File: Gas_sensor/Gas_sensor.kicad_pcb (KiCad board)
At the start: 2 copper layers, 143 parts, among them J1 Conn_02x02_Counter_Clockwise, J2 Conn_01x04, J3 Conn_01x10, J4 Conn_01x01, J5 Conn_01x01, Q1 DMC1229UFDB, Q2 DMC1229UFDB, Q3 Q_NMOS_GSD, Q4 Q_NMOS_GSD, Q5 Q_NMOS_GSD, Q6 Q_NMOS_GSD, SW1 SW_Push, SW10 SW_Push, SW11 SW_Push, SW12 SW_Push, SW2 SW_Push, SW3 SW_Push, SW4 SW_Push, SW5 SW_Push, SW6 SW_Push, SW7 SW_Push, SW8 SW_Push, SW9 SW_Push, U1 LPV511, U10 MCP1700-3302E_SOT23, U11 STM32F401CCUx, U12 TMP117, U13 TPS63070, U14 TPS79333-EP, U15 REG102GA, U2 LPV511, U3 MCP47CMB22, U4 MCP6V71, U5 LPV511, U6 MCP6V71, U7 MCP6V71, U8 MCP6V71, U9 ADS1115IDGS, Y1 25MHz

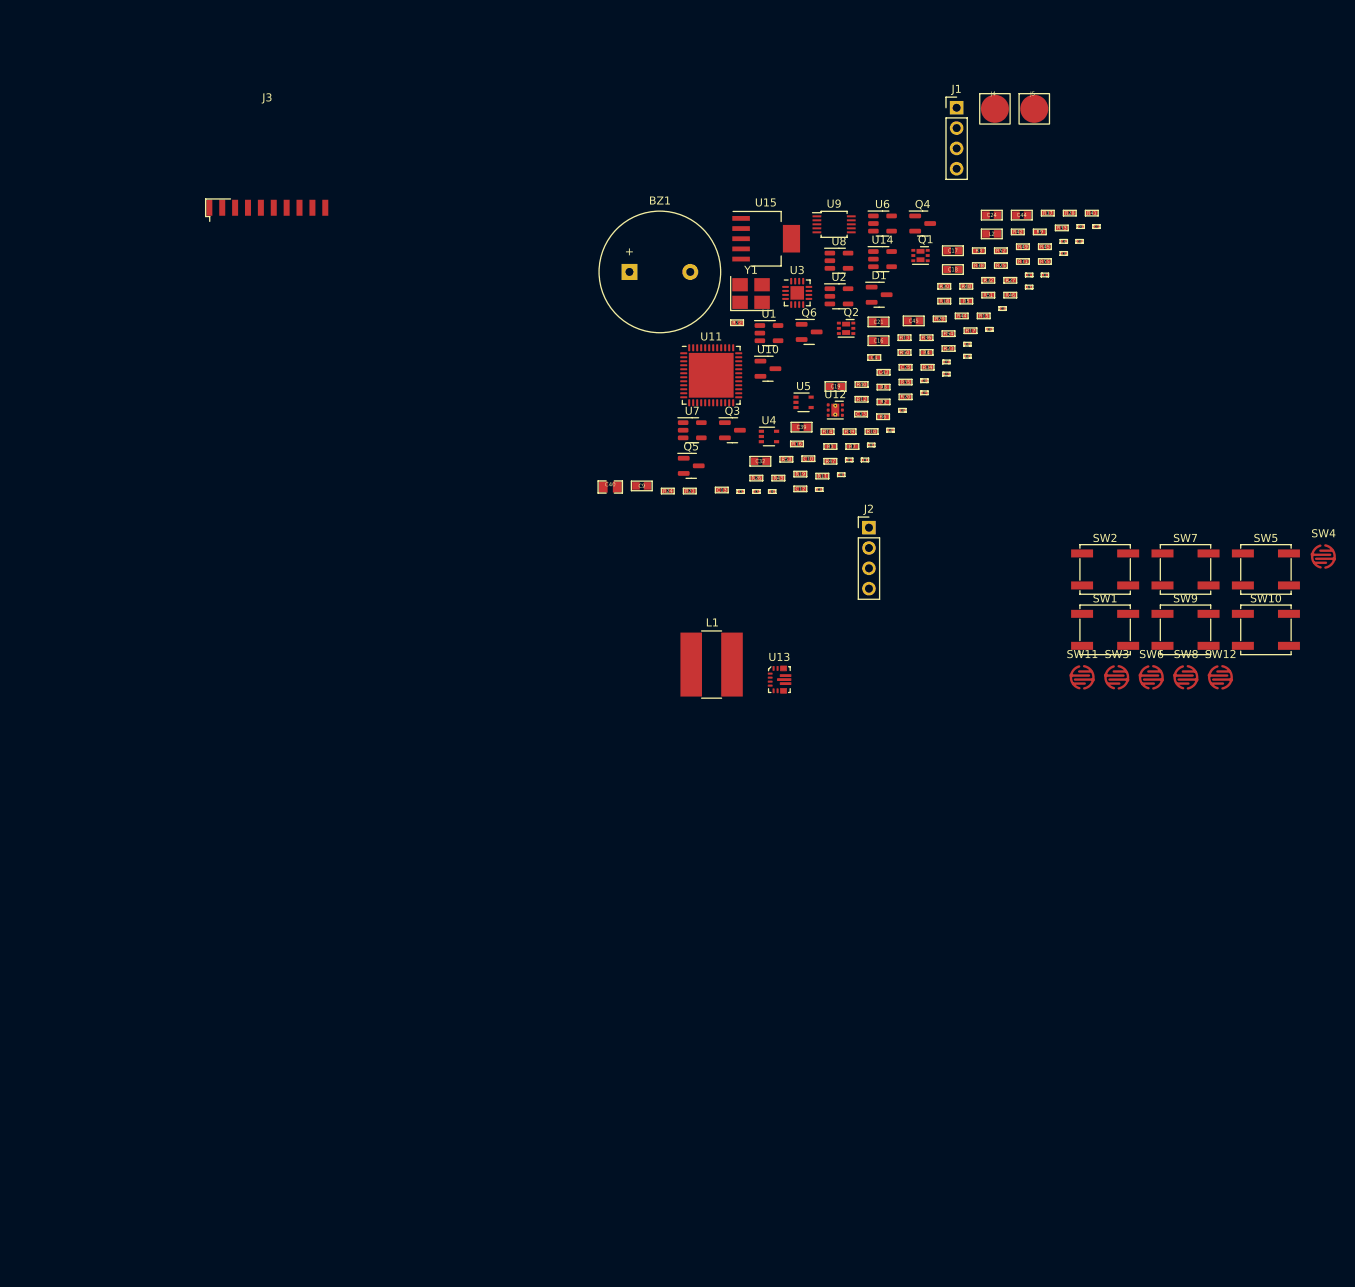
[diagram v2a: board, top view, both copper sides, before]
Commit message: Update layout, place switch
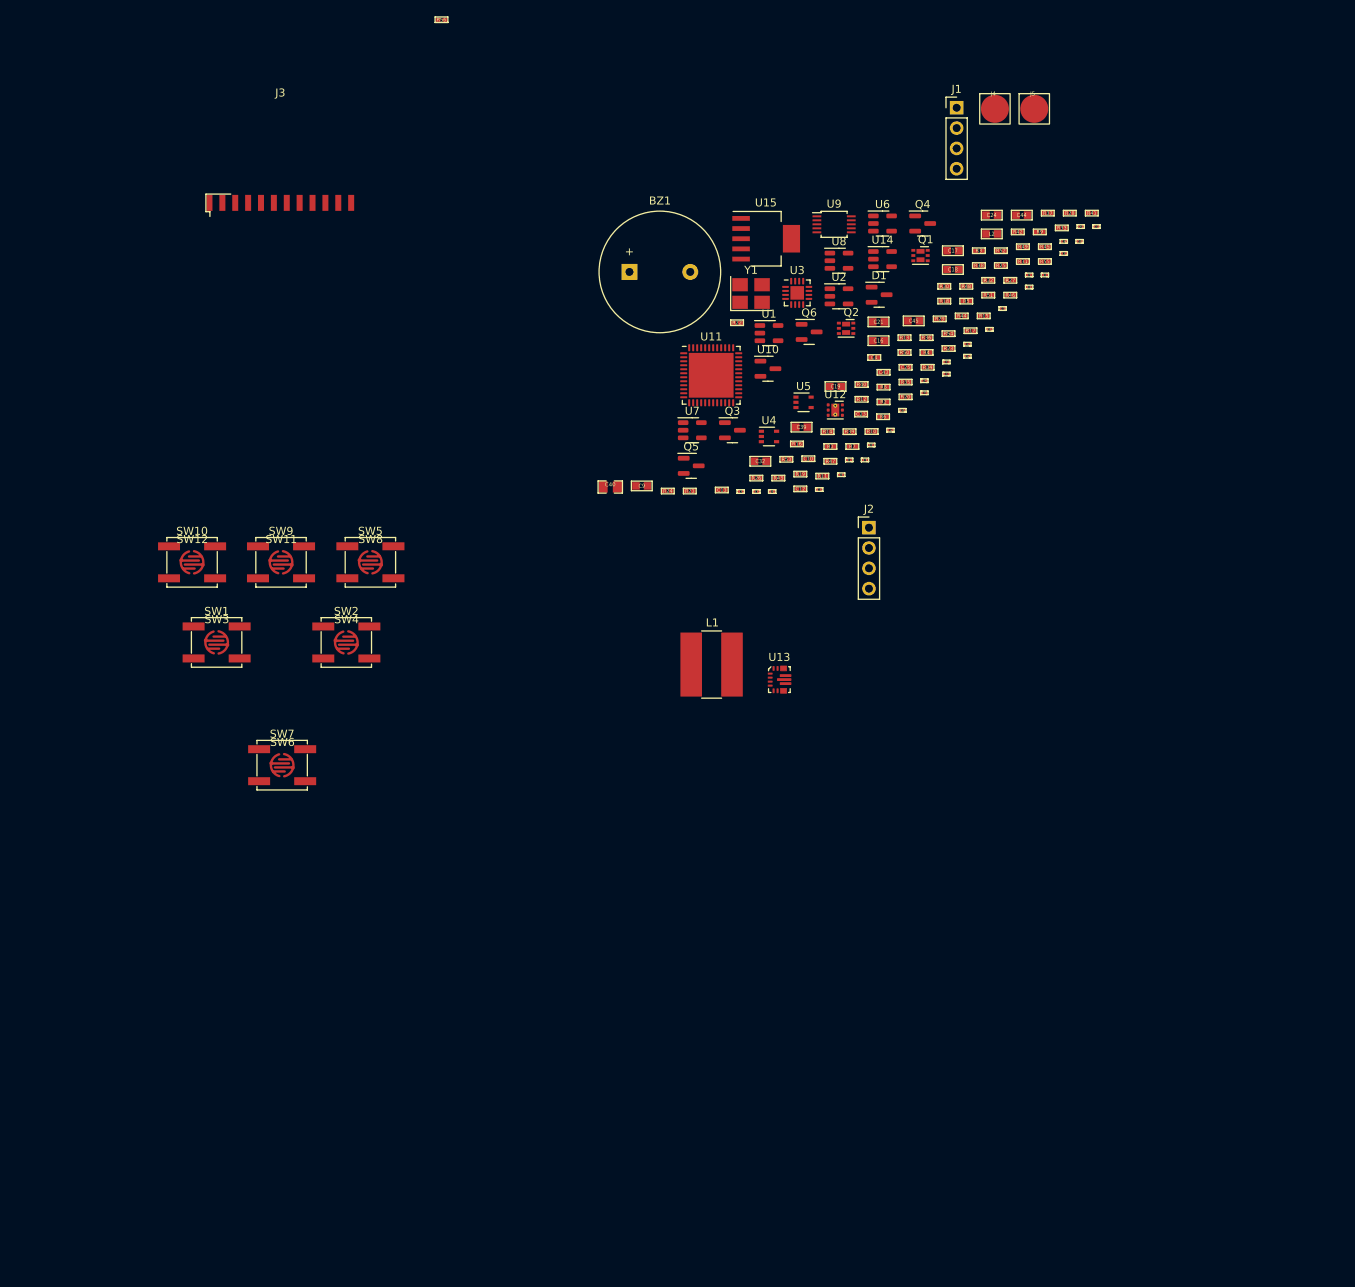
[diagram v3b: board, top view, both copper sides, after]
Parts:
- added R56: nc, Yame_library:SM0402-MR, F.Cu at (75.9, 23.7)
- J3: footprint Yame_library:LCD_Contact_1x10_P2.54mm -> Yame_library:LCD_Contact_1x12_P2.54mm
- moved SW10 134.5 mm to (44.8, 91.5)
- moved SW12 129.3 mm to (44.8, 91.5)
- moved SW4 122.6 mm to (64.0, 101.5)
- moved SW7 115.5 mm to (56.0, 116.9)
- moved SW9 113.4 mm to (55.9, 91.5)
- moved SW3 112.6 mm to (47.8, 101.5)
- moved SW5 111.9 mm to (67.0, 91.5)
- moved SW1 111.1 mm to (47.8, 101.5)
- moved SW6 109.2 mm to (56.0, 116.9)
- moved SW8 102.9 mm to (67.0, 91.5)
- moved SW11 101.2 mm to (55.9, 91.5)
- moved SW2 95.3 mm to (64.0, 101.5)
- moved J3 1.74 mm to (55.8, 46.6)
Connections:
- U11 pad 3: unconnected-(U11-Pad3) -> /Vseg6
- U11 pad 4: unconnected-(U11-Pad4) -> /Vseg7

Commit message: gas sensor : place components
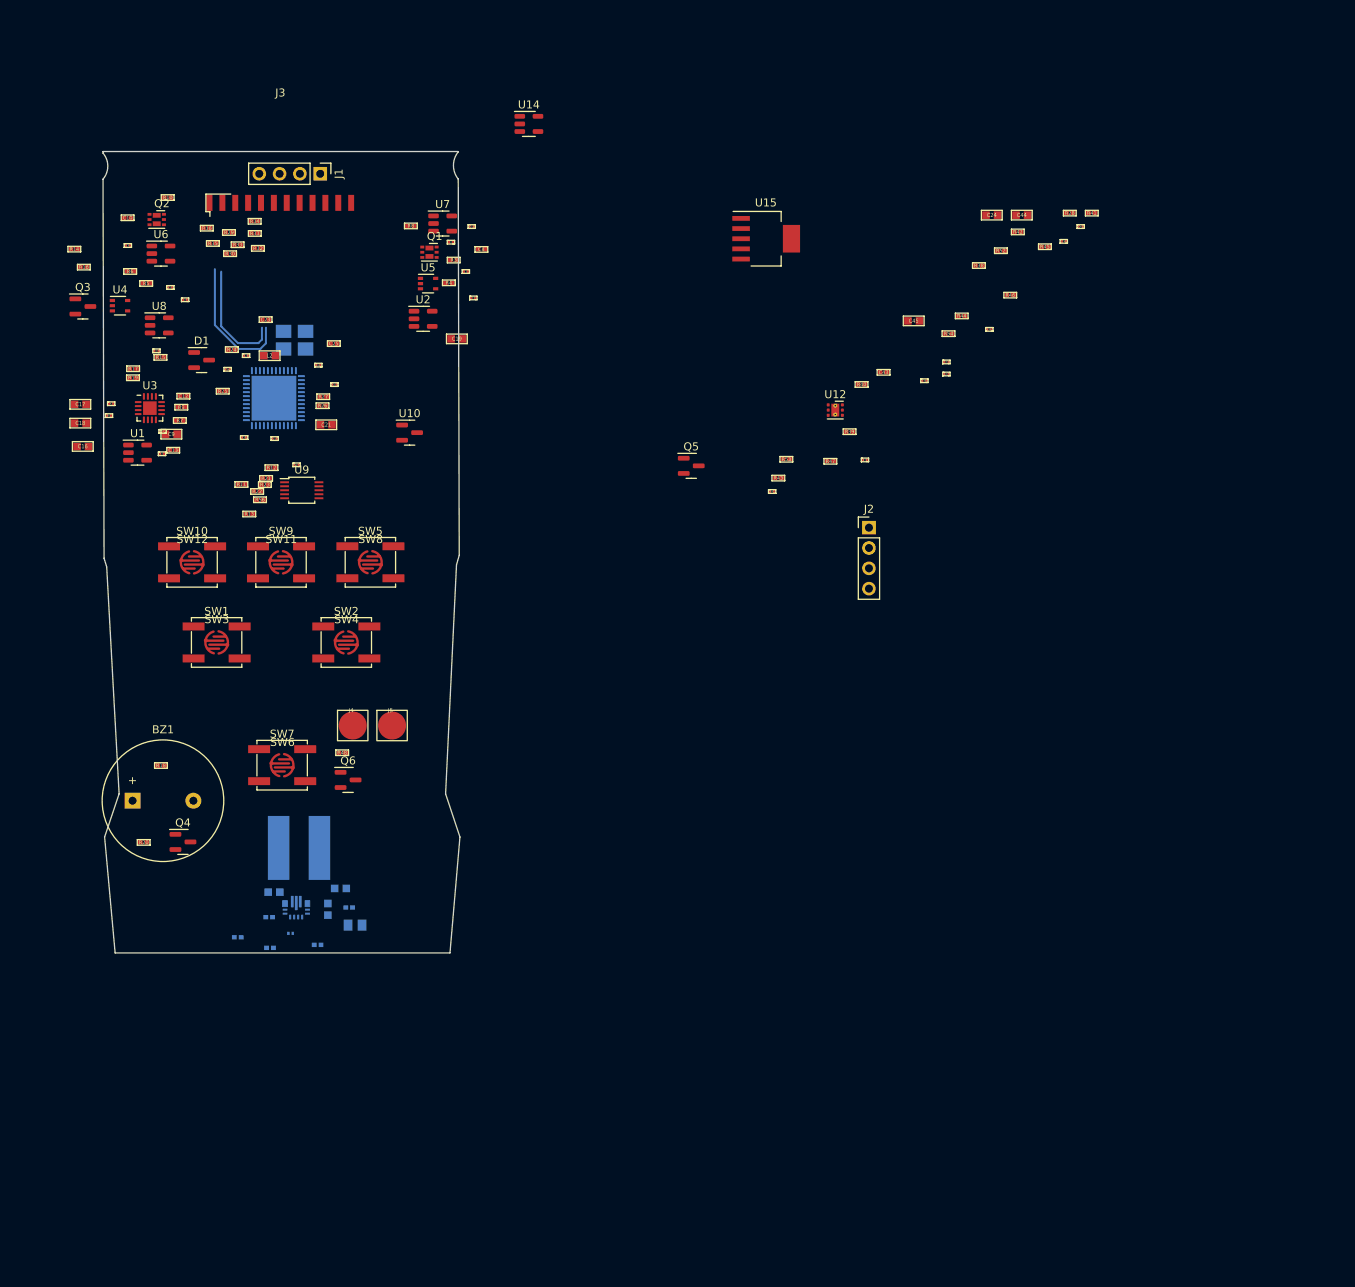
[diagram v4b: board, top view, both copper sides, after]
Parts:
- added C46: 10u, Yame_library:SM0603-MR, B.Cu at (63.3, 132.3)
- C32, C35, C39, C40, L1, R37, R49, R50, R51, R55, U11, U13, Y1: moved to B.Cu
- R1, R2: footprint Yame_library:SM0402-MR -> Yame_library:SM0201-MR
- moved R49 128.6 mm to (54.5, 139.7), turned to 180 degrees
- moved R55 124.7 mm to (60.5, 139.3), turned to 180 degrees
- moved R51 123.5 mm to (50.5, 138.4), turned to 180 degrees
- moved R37 123.1 mm to (64.4, 134.7), turned to 180 degrees
- moved Q4 120.5 mm to (43.6, 126.5)
- moved C14 116.2 mm to (40.3, 65.1)
- moved C5 114.8 mm to (41.1, 75.1)
- moved R18 113.8 mm to (40.9, 116.9)
- moved C6 112.7 mm to (36.7, 51.9)
- moved J4 111.3 mm to (64.8, 111.9)
- moved J5 111.3 mm to (69.8, 111.9)
- moved C17 110.7 mm to (30.8, 71.8)
- moved C18 110.7 mm to (30.8, 74.1)
- moved R20 110.3 mm to (38.7, 126.5)
- moved R9 109.5 mm to (43.4, 72.1)
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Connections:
- J1 pad 1: GND -> Net-(J1-Pad1)
- J1 pad 2: Net-(J1-Pad2) -> GND
- J1 pad 3: Net-(J1-Pad3) -> GND
- J1 pad 4: GND -> Net-(J1-Pad4)
- Q1 pad 3: Net-(J1-Pad2) -> Net-(J1-Pad1)
- Q1 pad 8: Net-(J1-Pad2) -> Net-(J1-Pad1)
- Q2 pad 3: Net-(J1-Pad3) -> Net-(J1-Pad4)
- Q2 pad 8: Net-(J1-Pad3) -> Net-(J1-Pad4)
- U7 pad 3: Net-(J1-Pad2) -> Net-(J1-Pad1)
- U8 pad 3: Net-(J1-Pad3) -> Net-(J1-Pad4)
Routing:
- net Net-(C26-Pad1): track 0.00 -> 16.9 mm
- net /Vcomm3: track 0.00 -> 14.5 mm
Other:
- board outline added: 44.6 x 100.2 mm
- copper layers 2 -> 4
- rule pad_to_mask_clearance: 0.2 -> 0.1

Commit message: update layout
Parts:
- removed C27: 100n, Yame_library:SM0201-MR
- removed D1: BAT54C, Package_TO_SOT_SMD:SOT-23
- C12, C13, C15, C19, C2, C20, C21, C22, C23, C24, C25, C26, C28, C29, C3, C30, C31, C4, C41, C42, C43, C44, C45, C5, C7, C9, J4, J5, L2, Q1, Q4, Q5, Q6, R1, R11, R12, R13, R18, R2, R20, R21, R22, R23, R25, R26, R27, R28, R29, R3, R30, R31, R32, R33, R34, R35, R36, R4, R40, R41, R42, R48, R56, R7, R8, R9, U1, U10, U12, U14, U15, U2, U3, U5, U7, U9: moved to B.Cu
- C16, C17, C18: footprint Yame_library:SM0603-MR -> Yame_library:SM0402-MR; moved to B.Cu
- R17, R19: footprint Yame_library:SM0402-MR -> Yame_library:SM0201-MR
- R24: footprint Yame_library:SM0402-MR -> Yame_library:SM0201-MR; moved to B.Cu
- Y1: footprint Oscillator:Oscillator_SMD_Abracon_ASE-4Pin_3.2x2.5mm_HandSoldering -> Crystal:Crystal_SMD_3225-4Pin_3.2x2.5mm
- moved R41 113.4 mm to (49.5, 83.2), turned to 90 degrees
- moved C44 109.5 mm to (57.9, 109.5), turned to 180 degrees
- moved C41 109.0 mm to (54.0, 88.3), turned to -90 degrees
- moved R42 103.3 mm to (49.5, 81.2), turned to 90 degrees
- moved C24 97.4 mm to (60.2, 96.5), turned to 90 degrees
- moved R28 88.1 mm to (67.5, 62.1), turned to -90 degrees
- moved C31 80.7 mm to (65.5, 79.4), turned to -90 degrees
- moved R40 80.6 mm to (49.5, 85.1), turned to 90 degrees
- moved C45 80.4 mm to (59.7, 89.5), turned to 90 degrees
- moved U15 79.5 mm to (57.3, 104.1), turned to 90 degrees
- moved C43 76.2 mm to (57.4, 86.8), turned to 180 degrees
- moved Q4 71.0 mm to (50.3, 55.7), turned to 180 degrees
- moved C42 68.1 mm to (54.5, 109.1), turned to 180 degrees
- moved Q5 60.6 mm to (46.5, 80.8), turned to 180 degrees
- moved U14 60.5 mm to (56.7, 89.2)
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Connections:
- C26 pad 1: Net-(C26-Pad1) -> +3V3
- U11 pad 1: Net-(C26-Pad1) -> +3V3
- U11 pad 20: unconnected-(U11-Pad20) -> /~{RDY}
- U11 pad 39: unconnected-(U11-Pad39) -> /APO
- U11 pad 46: /APO -> unconnected-(U11-Pad46)
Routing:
- net /Buzzer_EN: track 0.00 -> 53.2 mm
- net /Vcomm0: track 0.00 -> 27.5 mm
- net /Vcomm1: track 0.00 -> 27.0 mm
- net Net-(BZ1-Pad2): track 0.00 -> 25.1 mm
- net /Vseg0: track 0.00 -> 17.8 mm, vias 0 -> 1
- net Net-(C26-Pad1): track 16.9 -> 0.00 mm
- net /Vseg1: track 0.00 -> 13.5 mm
- net /Vseg5: track 0.00 -> 13.1 mm
- net /Vseg3: track 0.00 -> 12.6 mm
- net /Vseg4: track 0.00 -> 12.3 mm
- net /Vseg2: track 0.00 -> 12.3 mm
- net Net-(C23-Pad1): track 0.00 -> 12.1 mm
- net /Vcomm3: track 14.5 -> 24.7 mm
- net Net-(C25-Pad1): track 0.00 -> 6.73 mm
- net Net-(C20-Pad1): track 0.00 -> 2.59 mm
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
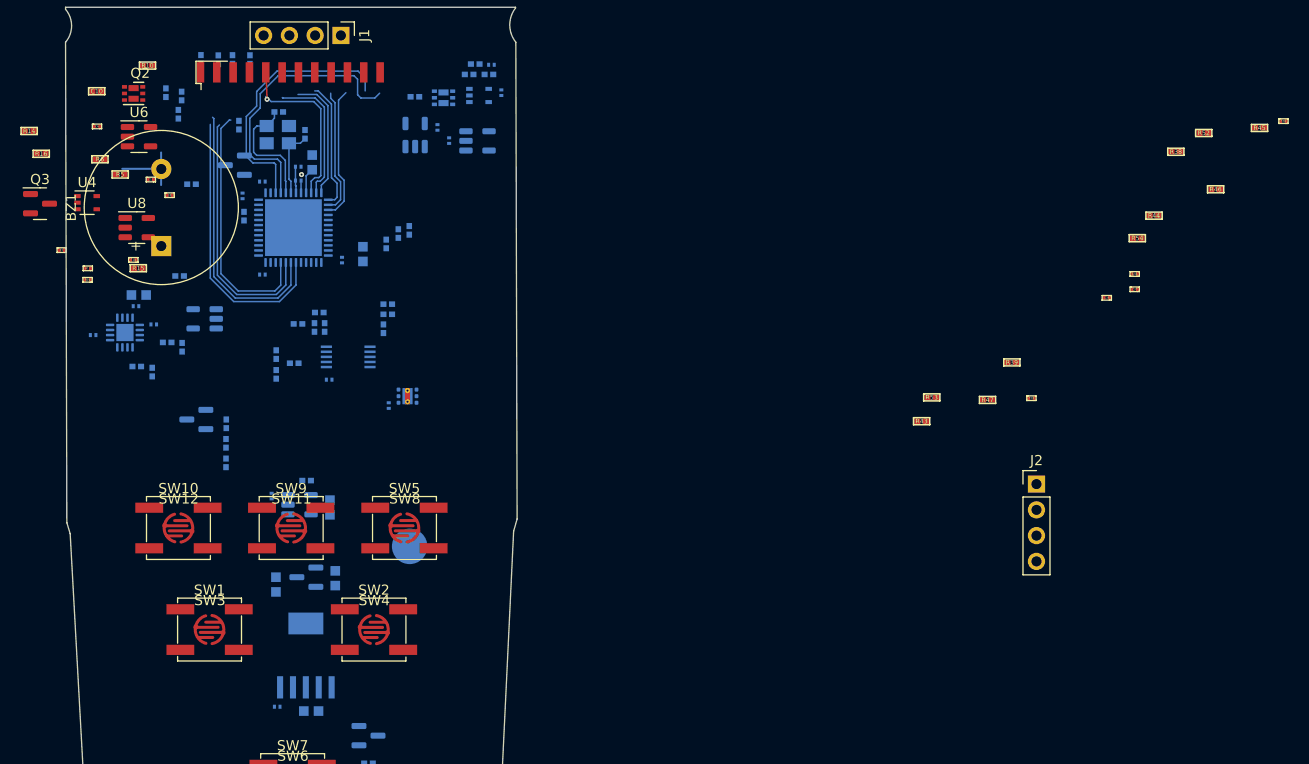
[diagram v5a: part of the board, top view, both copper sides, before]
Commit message: Gas sensor : update layout
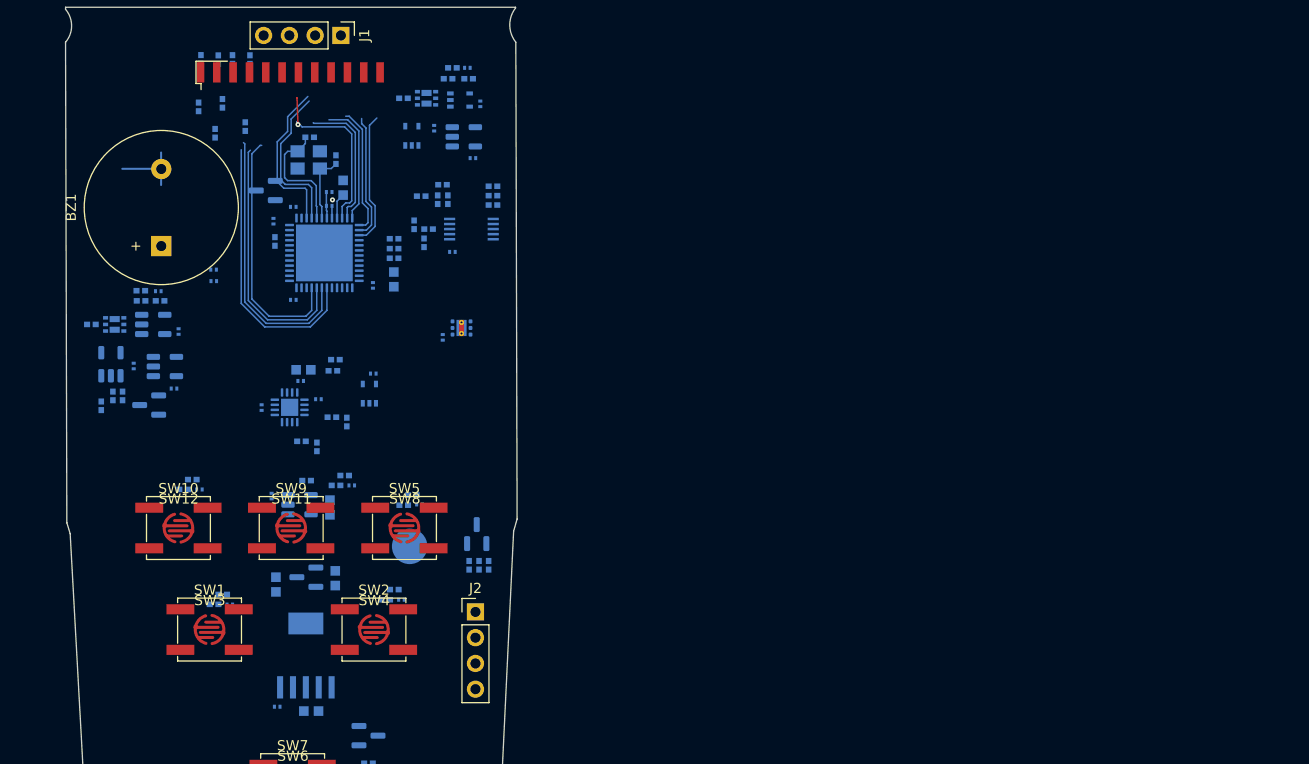
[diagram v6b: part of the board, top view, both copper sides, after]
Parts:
- C1, C10, C11, C14, C33, C34, C36, C37, C38, C6, C8, Q2, Q3, R10, R14, R15, R16, R17, R19, R38, R39, R43, R44, R45, R46, R47, R5, R52, R53, R54, R6, U6, U8: moved to B.Cu
- U1, U2: footprint Package_TO_SOT_SMD:SOT-23-5 -> Package_TO_SOT_SMD:SOT-353_SC-70-5
- U4: footprint Package_TO_SOT_SMD:SOT-353_SC-70-5 -> Package_TO_SOT_SMD:SOT-23-5; moved to B.Cu
- moved C38 112.9 mm to (46.8, 87.7)
- moved R38 103.6 mm to (49.1, 98.0), turned to 180 degrees
- moved R54 97.2 mm to (45.3, 87.7)
- moved R45 91.0 mm to (67.8, 88.2), turned to 180 degrees
- moved R46 90.4 mm to (61.1, 86.3), turned to 180 degrees
- moved R52 87.0 mm to (67.0, 89.2)
- moved R44 84.7 mm to (65.2, 98.6)
- moved C33 81.6 mm to (49.8, 99.0)
- moved C37 79.6 mm to (61.9, 87.3)
- moved C34 79.1 mm to (66.8, 98.6)
- moved R47 78.8 mm to (46.1, 86.7), turned to 180 degrees
- moved R43 72.1 mm to (48.3, 99.0)
- moved C36 70.8 mm to (68.5, 89.2)
- moved R39 64.9 mm to (66.0, 97.6), turned to 180 degrees
- moved R53 59.4 mm to (60.3, 87.3)
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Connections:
- U6 pad 2: +9V -> GND
- U6 pad 3: Net-(Q2-Pad4) -> Net-(Q2-Pad6)
- U6 pad 4: Net-(Q2-Pad6) -> Net-(Q2-Pad4)
- U6 pad 5: GND -> +9V
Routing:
- net /Buzzer_EN: track 53.2 -> 31.0 mm
